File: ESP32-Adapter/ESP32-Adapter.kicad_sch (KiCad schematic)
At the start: 17 parts, among them J10 Barrel_Jack, J12 Conn_01x05, J13 Conn_01x05, J2 Conn_01x03, J3 Conn_01x03, J5 Conn_01x03, U1 ESP32-C5-DevKitC-1, U2 LM317_TO-263, U3 Adafruit CANPAL, U4 ADAFRUIT INA219 BREAKOUT

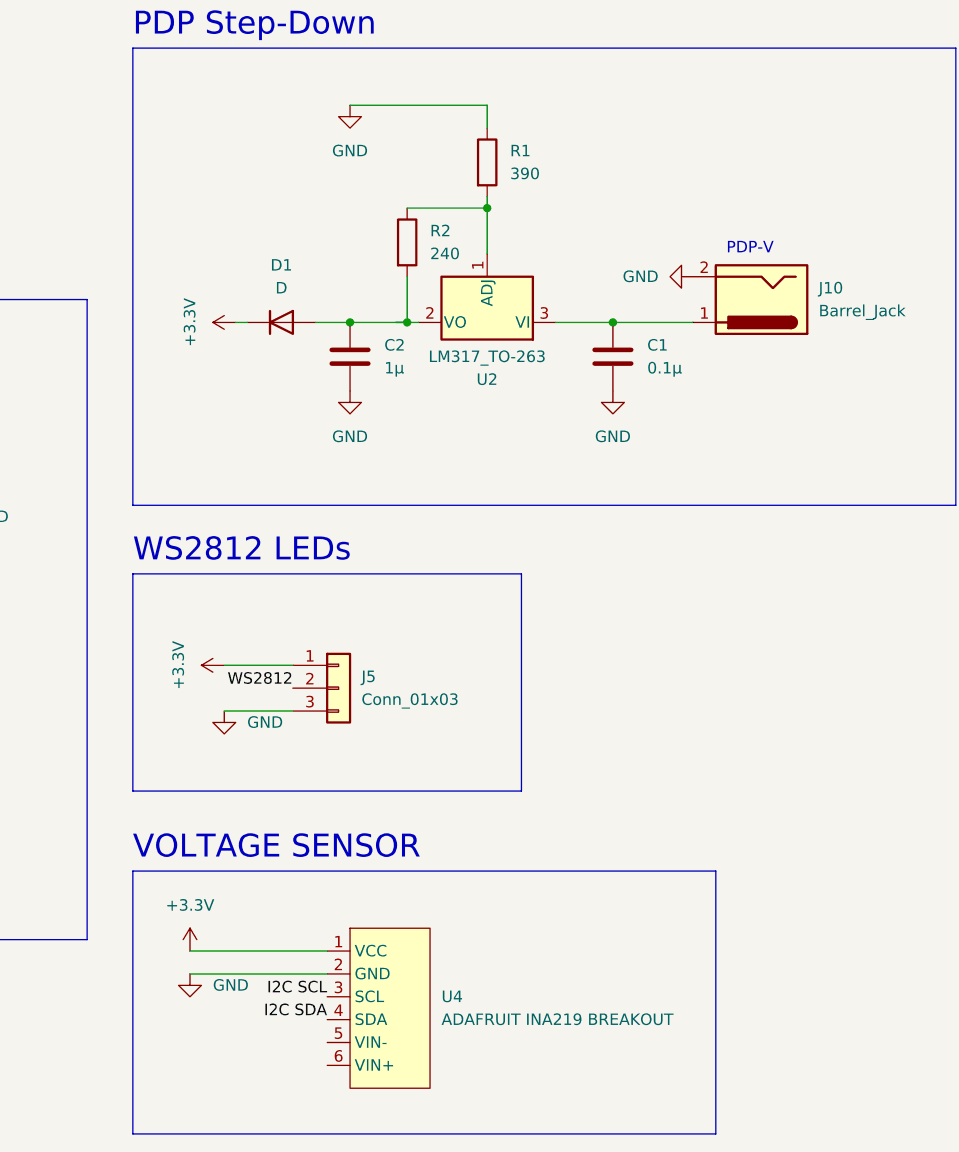
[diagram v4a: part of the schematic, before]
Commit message: Update Schematic
Added annotations. Modified value of R1 in voltage-stepdown circuit. Added footprint for diode and changed footprint for LM317
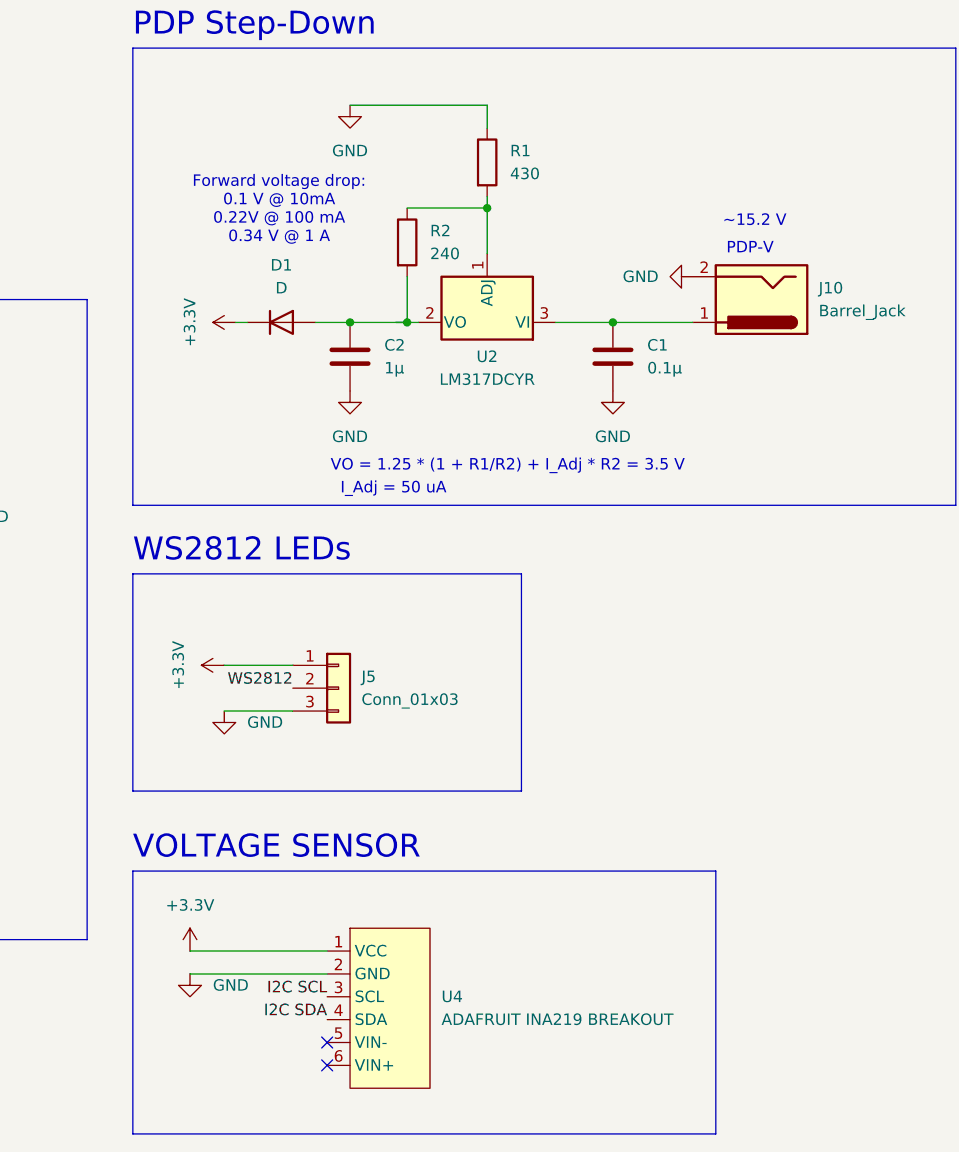
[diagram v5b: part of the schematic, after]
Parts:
- D1: footprint Diode_SMD:D_0805_2012Metric -> footprints:USC_TOS
- R1: value 390 -> 430
- U2: value LM317_TO-263 -> LM317DCYR; footprint Package_TO_SOT_SMD:TO-263-2 -> Package_TO_SOT_SMD:SOT-223
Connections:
- no-connect marks 14 -> 16
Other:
- note added: "Forward voltage drop: 0.1 V @ 10mA 0.22V @ 100 mA 0.34 V @ 1 A"
- note added: "I_Adj = 50 uA"
- note added: "VO = 1.25 * (1 + R1/R2) + I_Adj * R2 = 3.5 V"
- note added: "~15.2 V"
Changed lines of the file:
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@@
 		)
 	)
+	(text "~15.2 V\n"
+		(exclude_from_sim no)
+		(at 420.878 157.734 0)
+		(effects
+			(font
+				(size 1.27 1.27)
+			)
+		)
+	)
 	(text "vash the stampede\n"
 		(exclude_from_sim no)
@@
 		)
 	)
+	(text "Forward voltage drop: \n0.1 V @ 10mA\n0.22V @ 100 mA\n0.34 V @ 1 A"
+		(exclude_from_sim no)
+		(at 368.046 156.464 0)
+		(effects
+			(font
+				(size 1.27 1.27)
+			)
+		)
+	)
 	(text "Vcc"
 		(exclude_from_sim no)
@@
 		)
 	)
+	(text "I_Adj = 50 uA"
+		(exclude_from_sim no)
+		(at 380.746 187.452 0)
+		(effects
+			(font
+				(size 1.27 1.27)
+			)
+		)
+	)
 	(text "PDP Step-Down\n"
 		(exclude_from_sim no)
@@
 		)
 	)
+	(text "VO = 1.25 * (1 + R1/R2) + I_Adj * R2 = 3.5 V\n"
+		(exclude_from_sim no)
+		(at 393.446 184.912 0)
+		(effects
+			(font
+				(size 1.27 1.27)
+			)
+		)
+	)
 	(text "CANPal\n"
 		(exclude_from_sim no)
@@
 	)
 	(no_connect
+		(at 373.38 251.46)
+	)
+	(no_connect
 		(at 316.23 219.71)
 	)
@@
 	)
 	(no_connect
+		(at 373.38 248.92)
+	)
+	(no_connect
 		(at 210.82 234.95)
 	)
@@
 			)
 		)
-		(property "Value" "390"
+		(property "Value" "430"
 			(at 393.7 152.3999 0)
 			(effects
@@
 		(fields_autoplaced yes)
 		(property "Reference" "U2"
-			(at 391.16 175.26 0)
+			(at 391.16 172.72 0)
 			(effects
 				(font
@@
 			)
 		)
-		(property "Value" "LM317_TO-263"
-			(at 391.16 172.72 0)
+		(property "Value" "LM317DCYR"
+			(at 391.16 175.26 0)
 			(effects
 				(font
@@
 			)
 		)
-		(property "Footprint" "Package_TO_SOT_SMD:TO-263-2"
+		(property "Footprint" "Package_TO_SOT_SMD:SOT-223"
 			(at 391.16 175.26 0)
 			(effects
@@
 			)
 		)
-		(property "Description" "1.5A 35V Adjustable Linear Regulator, TO-263"
+		(property "Description" "1.5A 35V Adjustable Linear Regulator, SOT-223"
 			(at 391.16 168.91 0)
 			(effects
@@
 			)
 		)
-		(property "Footprint" "Diode_SMD:D_0805_2012Metric"
+		(property "Footprint" "footprints:USC_TOS"
 			(at 368.3 168.91 0)
 			(effects
@@
 			)
 		)
-		(property "Datasheet" "~"
+		(property "Datasheet" "https://toshiba.semicon-storage.com/info/CUS15S30_datasheet_en_20140407.pdf?did=13655&prodName=CUS15S30"
 			(at 368.3 168.91 0)
 			(effects

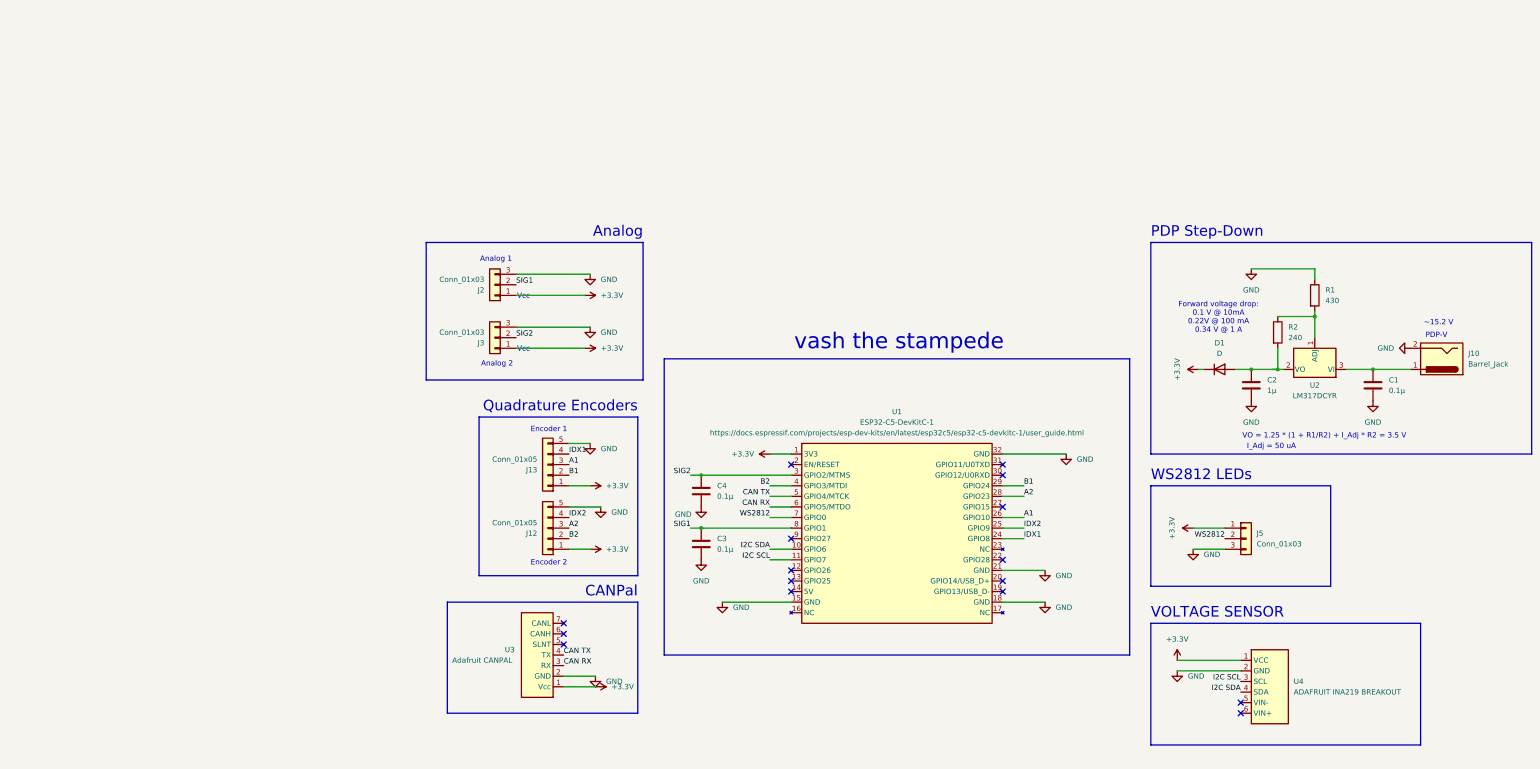
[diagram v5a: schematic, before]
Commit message: Add GND Plane
Added GND Plane. Sized down PCB. Added some 3D models.
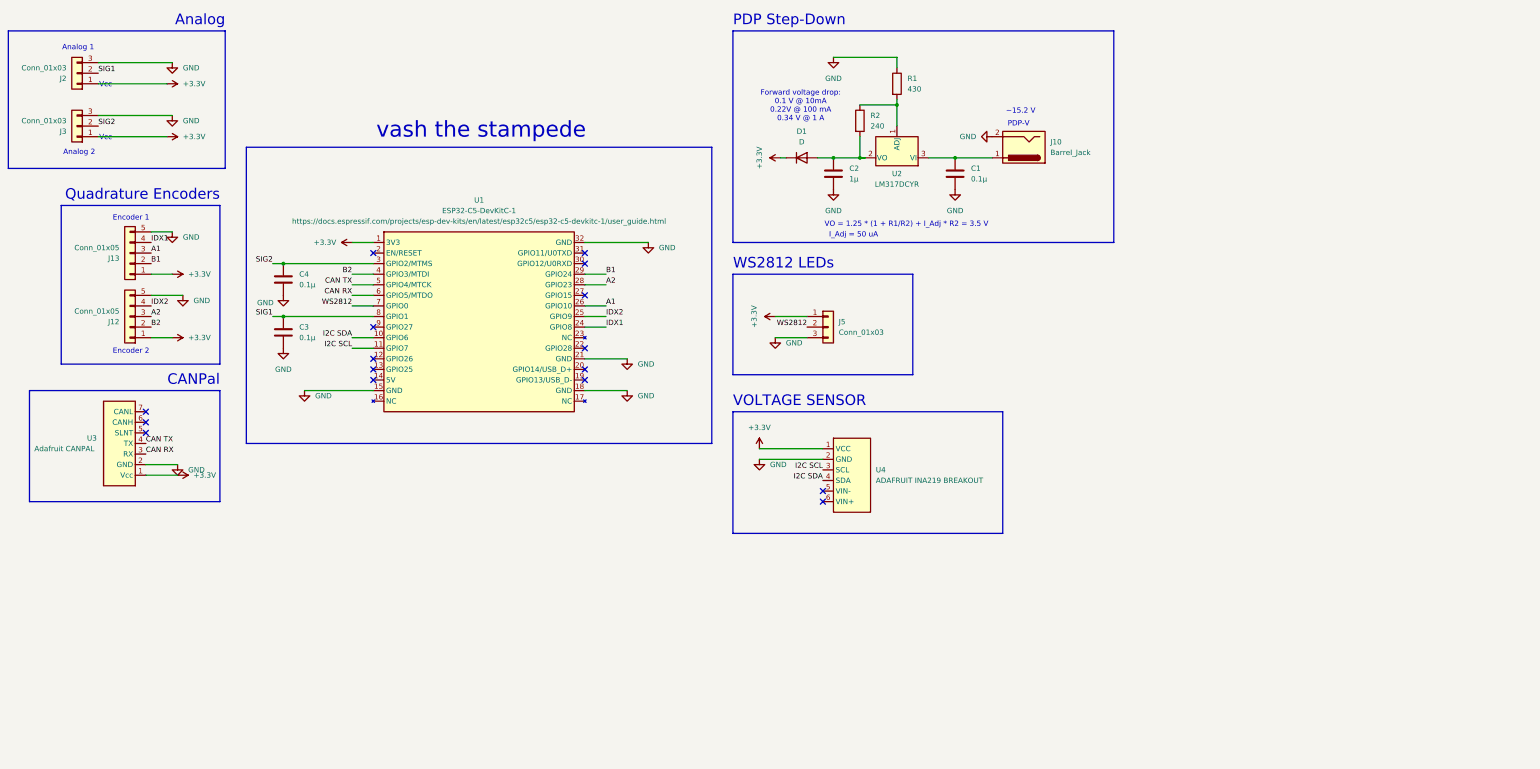
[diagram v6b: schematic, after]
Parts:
- U1: footprint PCM_Espressif:ESP32-C5-DevKitC-1 -> footprints:ESP32-C5-DevKitC-1; symbol PCM_Espressif:ESP32-C5-DevKitC-1 -> symbols:ESP32-C5-DevKitC-1
- U2: footprint Package_TO_SOT_SMD:SOT-223 -> Package_TO_SOT_SMD:SOT-223-3_TabPin2
- U3: footprint Audio_Module:canpal -> footprints:canpal; symbol Interface_CAN_LIN:CANPAL -> symbols:CANPAL
- U4: footprint Audio_Module:INA219 Breakout -> footprints:INA219 Breakout; symbol Analog_ADC:INA219_ADAFRUIT -> symbols:INA219_ADAFRUIT
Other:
- title: (none) -> ESP Stampede
- moved on the sheet: C1, C2, C3, C4, D1, J10, J12, J13, J2, J3, J5, R1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
